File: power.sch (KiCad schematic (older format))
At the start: 5 parts

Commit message: added voltage regulators and FT231XS to drone library
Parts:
- removed J?: MOTOR_DRIVER, symbol Connector:Conn_01x02_Male
- removed U?: D36V50F5, Drone:D36V50F5, symbol Drone:D36V50F5
- added J?: XT60PW-M, Drone:XT60PW-M, symbol Drone:XT60PW-M
- added U?: D36V28F3, symbol Drone:D36V28F3
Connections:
- net labels added: 3V3, 5V
- wire segments 9 -> 35
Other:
- note added: "1. PG low battery indicator? (open drain and external pull up resistor is required)\n2. Enabled by default so EN shouldnt be wired?\n3. any capacitors missing?"
- note added: "Motor_Driver_Connector"
- moved on the sheet: SSR?, U?
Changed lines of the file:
@@
 $Descr A4 11693 8268
 encoding utf-8
-Sheet 4 6
+Sheet 4 5
 Title ""
 Date ""
@@
 L Drone:CMX60D20 SSR?
 U 1 1 5E3F8AD0
-P 4650 1150
+P 5900 1500
 AR Path="/5E3F8AD0" Ref="SSR?"  Part="1"
 AR Path="/5E3E92F4/5E3F8AD0" Ref="U?"  Part="1"
-F 0 "U?" H 4450 1300 50  0000 C CNN
-F 1 "CMX60D20" H 4600 1200 50  0000 C CNN
-F 2 "Drone:CMX60D20" H 4550 1150 50  0001 L BNN
-F 3 "https://www.tme.com/Document/b27c1a9b330ca081d5500ebe72e3b05d/c_m_x.pdf" H 4650 1150 50  0001 C CNN
-	1    4650 1150
+F 0 "U?" H 5700 1650 50  0000 C CNN
+F 1 "CMX60D20" H 5850 1550 50  0000 C CNN
+F 2 "Drone:CMX60D20" H 5800 1500 50  0001 L BNN
+F 3 "https://www.tme.com/Document/b27c1a9b330ca081d5500ebe72e3b05d/c_m_x.pdf" H 5900 1500 50  0001 C CNN
+	1    5900 1500
 	1    0    0    -1
 $EndComp
-Text Label 3700 1300 0    50   ~ 0
+Text Label 4950 1650 0    50   ~ 0
 GND
 Wire Wire Line
-	3700 1300 4200 1300
-Text Label 3700 1200 0    50   ~ 0
+	4950 1650 5450 1650
+Text Label 4950 1550 0    50   ~ 0
 GPIO_3V3
-Text Label 3700 850  0    50   ~ 0
+Text Label 4950 1200 0    50   ~ 0
 11V1
-$Comp
-L Connector:Conn_01x02_Male J?
-U 1 1 5E3F8ADC
-P 5450 1400
-F 0 "J?" V 5512 1444 50  0000 L CNN
-F 1 "MOTOR_DRIVER" V 5603 1444 50  0000 L CNN
-F 2 "" H 5450 1400 50  0001 C CNN
-F 3 "~" H 5450 1400 50  0001 C CNN
-	1    5450 1400
-	-1   0    0    1
-$EndComp
-Text Label 5100 1950 1    50   ~ 0
+Text Label 6500 1150 3    50   ~ 0
 GND
 $Comp
 L Drone:XT60PW-M J?
 U 1 1 5E3FF515
-P 1150 1100
+P 1600 4000
 AR Path="/5E3FF515" Ref="J?"  Part="1"
 AR Path="/5E3E92F4/5E3FF515" Ref="J?"  Part="1"
-F 0 "J?" H 1043 733 50  0000 C CNN
-F 1 "XT60PW-M" H 1043 824 50  0000 C CNN
-F 2 "Drone:XT60PW-M" H 1100 1400 50  0001 L BNN
-F 3 "https://www.snapeda.com/parts/XT60PW-M%20/AMASS/datasheet/" H 1100 1200 50  0001 L BNN
-	1    1150 1100
+F 0 "J?" H 1493 3633 50  0000 C CNN
+F 1 "XT60PW-M" H 1493 3724 50  0000 C CNN
+F 2 "Drone:XT60PW-M" H 1550 4300 50  0001 L BNN
+F 3 "https://www.snapeda.com/parts/XT60PW-M%20/AMASS/datasheet/" H 1550 4100 50  0001 L BNN
+	1    1600 4000
 	-1   0    0    1
 $EndComp
-Text Label 1850 1000 2    50   ~ 0
+Text Label 2300 3900 2    50   ~ 0
 11V1
 Wire Wire Line
-	1850 1200 1550 1200
-Text Label 1850 1200 2    50   ~ 0
+	2300 4100 2000 4100
+Text Label 2300 4100 2    50   ~ 0
 GND
 Wire Wire Line
-	1850 1000 1550 1000
+	2300 3900 2000 3900
 Wire Wire Line
-	4200 1200 3700 1200
+	5450 1550 4950 1550
 Wire Wire Line
-	5100 850  5100 1200
+	6350 1200 6350 1550
 Wire Wire Line
-	3700 850  5100 850
+	4950 1200 6350 1200
 Wire Wire Line
-	5100 1300 5250 1300
-Wire Wire Line
-	5250 1400 5100 1400
-Wire Wire Line
-	5100 1400 5100 1950
+	6350 1650 6500 1650
 $Comp
 L Drone:D36V50F5 U?
 U 1 1 5E3ABE9B
-P 2650 3000
-AR Path="/5E3ABE9B" Ref="U?"  Part="1"
-AR Path="/5E3E92F4/5E3ABE9B" Ref="U?"  Part="1"
-F 0 "U?" H 2650 2577 50  0000 C CNN
-F 1 "D36V50F5" H 2650 2486 50  0000 C CNN
-F 2 "Drone:D36V50F5" H 2600 2950 50  0001 C CNN
-F 3 "https://www.pololu.com/product/4091" H 2600 2950 50  0001 C CNN
-	1    2650 3000
+P 5150 3700
+F 0 "U?" H 5150 3650 50  0000 C CNN
+F 1 "D36V50F5" H 5150 3750 50  0000 C CNN
+F 2 "Drone:D36V50F5" H 5100 3650 50  0001 C CNN
+F 3 "https://www.pololu.com/product/4091" H 5100 3650 50  0001 C CNN
+	1    5150 3700
 	1    0    0    -1
 $EndComp
+Text Label 4300 3600 0    50   ~ 0
+11V1
+Text Label 6650 3550 0    50   ~ 0
+11V1
+Wire Wire Line
+	6650 3550 7050 3550
+Text Label 6800 4000 1    50   ~ 0
+GND
+Wire Wire Line
+	6800 3750 7050 3750
+Wire Wire Line
+	6800 3750 6800 4000
+Text Label 6000 3600 2    50   ~ 0
+5V
+Wire Wire Line
+	5700 3600 5750 3600
+Text Label 5100 4800 1    50   ~ 0
+GND
+Wire Wire Line
+	5400 4150 5400 4300
+Wire Wire Line
+	5400 4300 5250 4300
+Wire Wire Line
+	5100 4300 5100 4400
+Wire Wire Line
+	5100 4150 5100 4300
+Connection ~ 5100 4300
+Wire Wire Line
+	5250 4150 5250 4300
+Connection ~ 5250 4300
+Wire Wire Line
+	5250 4300 5100 4300
+Wire Wire Line
+	4950 4150 4950 4400
+Wire Wire Line
+	4950 4400 5100 4400
+Connection ~ 5100 4400
+Wire Wire Line
+	5100 4400 5100 4800
+Wire Wire Line
+	4300 3600 4550 3600
+Wire Wire Line
+	4550 3600 4550 3800
+Wire Wire Line
+	4550 3800 4600 3800
+Connection ~ 4550 3600
+Wire Wire Line
+	4550 3600 4600 3600
+Wire Wire Line
+	5700 3800 5750 3800
+Wire Wire Line
+	5750 3800 5750 3600
+Connection ~ 5750 3600
+Wire Wire Line
+	5750 3600 6000 3600
+Text Notes 4750 5200 0    50   ~ 0
+1. PG low battery indicator? (open drain and external pull up resistor is required)\n2. Enabled by default so EN shouldnt be wired?\n3. any capacitors missing?
+Wire Wire Line
+	8150 3550 8400 3550
+Text Label 8400 3550 2    50   ~ 0
+3V3
 $Comp
-L Drone:D36V50F5 U?
-U 1 1 5E3AC357
-P 4950 3000
-AR Path="/5E3AC357" Ref="U?"  Part="1"
-AR Path="/5E3E92F4/5E3AC357" Ref="U?"  Part="1"
-F 0 "U?" H 4950 2577 50  0000 C CNN
-F 1 "D36V50F5" H 4950 2486 50  0000 C CNN
-F 2 "Drone:D36V50F5" H 4900 2950 50  0001 C CNN
-F 3 "https://www.pololu.com/product/4091" H 4900 2950 50  0001 C CNN
-	1    4950 3000
+L Drone:D36V28F3 U?
+U 1 1 5E3B18FA
+P 7600 3650
+F 0 "U?" H 7600 3750 50  0000 C CNN
+F 1 "D36V28F3" H 7600 3600 50  0000 C CNN
+F 2 "" H 7550 3600 50  0001 C CNN
+F 3 "https://www.pololu.com/product/3781" H 7550 3600 50  0001 C CNN
+	1    7600 3650
 	1    0    0    -1
 $EndComp
+Wire Wire Line
+	8150 3750 8150 4100
+Wire Wire Line
+	8150 4100 7050 4100
+Wire Wire Line
+	7050 4100 7050 3750
+Connection ~ 7050 3750
+Text HLabel 10900 6000 2    50   Output ~ 0
+5V
+Text HLabel 10900 6100 2    50   Output ~ 0
+3V3
+Text HLabel 10900 6200 2    50   Output ~ 0
+GND
+Wire Wire Line
+	10900 6000 10650 6000
+Wire Wire Line
+	10900 6100 10650 6100
+Wire Wire Line
+	10900 6200 10650 6200
+Text Label 10650 6200 0    50   ~ 0
+GND
+Text Label 10650 6100 0    50   ~ 0
+3V3
+Text Label 10650 6000 0    50   ~ 0
+5V
+$Comp
+L Drone:XT60PW-M J?
+U 1 1 5E4231A4
+P 6900 1550
+AR Path="/5E4231A4" Ref="J?"  Part="1"
+AR Path="/5E3E92F4/5E4231A4" Ref="J?"  Part="1"
+F 0 "J?" H 6793 1183 50  0000 C CNN
+F 1 "XT60PW-M" H 6793 1274 50  0000 C CNN
+F 2 "Drone:XT60PW-M" H 6850 1850 50  0001 L BNN
+F 3 "https://www.snapeda.com/parts/XT60PW-M%20/AMASS/datasheet/" H 6850 1650 50  0001 L BNN
+	1    6900 1550
+	1    0    0    -1
+$EndComp
+Wire Wire Line
+	6500 1150 6500 1450
+Text Notes 6650 1300 0    50   ~ 0
+Motor_Driver_Connector
 $EndSCHEMATC

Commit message: added connectors symbols and footprints
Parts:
- removed J? (x2): XT60PW-M, Drone:XT60PW-M, symbol Drone:XT60PW-M
- added J?: XT90PW-M, Drone:XT90PW-M, symbol Drone:XT90PW-M
- added J?: XT60PW-F_Vertical, Drone:AMASS_XT60-F_1x02_P7.20mm_Vertical, symbol Drone:XT60PW-F_Vertical
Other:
- note added: "TODO: \n2. check what top level components are necessary (voltage regulators & stepdown?)\n4. Replace motor driver 2 pin male connector with a proper connector\n5. Check connectors orientation\n"
- note removed: "TODO: \n1. batt connector to switch (maybe not)\n2. check what top level components are necessary (voltage regulators & stepdown?)\n3. CMX60D20 connection to motor board (double check symbol)\n4. Replace motor driver 2 pin male connector with a proper connector\n5. check XT60PW and CMX60D20 connections (connect to proper GPIO)"
- moved on the sheet: SSR?
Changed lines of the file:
@@
 $Descr A4 11693 8268
 encoding utf-8
-Sheet 2 6
+Sheet 6 6
 Title ""
 Date ""
@@
 Comment4 ""
 $EndDescr
-Text Notes 7750 1200 0    50   ~ 0
-TODO: \n1. batt connector to switch (maybe not)\n2. check what top level components are necessary (voltage regulators & stepdown?)\n3.  CMX60D20 connection to motor board (double check symbol)\n4. Replace motor driver 2 pin male connector with a proper connector\n5. check XT60PW and CMX60D20 connections (connect to proper GPIO)
+Text Notes 5950 1700 0    50   ~ 0
+TODO: \n2. check what top level components are necessary (voltage regulators & stepdown?)\n4. Replace motor driver 2 pin male connector with a proper connector\n5. Check connectors orientation\n
 $Comp
 L Drone:CMX60D20 SSR?
 U 1 1 5E3F8AD0
-P 5900 1500
+P 3300 1350
 AR Path="/5E3F8AD0" Ref="SSR?"  Part="1"
 AR Path="/5E3E92F4/5E3F8AD0" Ref="U?"  Part="1"
-F 0 "U?" H 5700 1650 50  0000 C CNN
-F 1 "CMX60D20" H 5850 1550 50  0000 C CNN
-F 2 "Drone:CMX60D20" H 5800 1500 50  0001 L BNN
-F 3 "https://www.tme.com/Document/b27c1a9b330ca081d5500ebe72e3b05d/c_m_x.pdf" H 5900 1500 50  0001 C CNN
-	1    5900 1500
+F 0 "U?" H 3100 1500 50  0000 C CNN
+F 1 "CMX60D20" H 3250 1400 50  0000 C CNN
+F 2 "Drone:CMX60D20" H 3200 1350 50  0001 L BNN
+F 3 "https://www.tme.com/Document/b27c1a9b330ca081d5500ebe72e3b05d/c_m_x.pdf" H 3300 1350 50  0001 C CNN
+	1    3300 1350
 	1    0    0    -1
 $EndComp
-Text Label 4950 1650 0    50   ~ 0
+Text Label 2350 1500 0    50   ~ 0
 GND
 Wire Wire Line
-	4950 1650 5450 1650
-Text Label 4950 1550 0    50   ~ 0
+	2350 1500 2850 1500
+Text Label 2350 1400 0    50   ~ 0
 GPIO_3V3
-Text Label 4950 1200 0    50   ~ 0
+Text Label 2350 1050 0    50   ~ 0
 11V1
-Text Label 6500 1150 3    50   ~ 0
+Text Label 3900 1000 3    50   ~ 0
 GND
-$Comp
-L Drone:XT60PW-M J?
-U 1 1 5E3FF515
-P 1600 4000
-AR Path="/5E3FF515" Ref="J?"  Part="1"
-AR Path="/5E3E92F4/5E3FF515" Ref="J?"  Part="1"
-F 0 "J?" H 1493 3633 50  0000 C CNN
-F 1 "XT60PW-M" H 1493 3724 50  0000 C CNN
-F 2 "Drone:XT60PW-M" H 1550 4300 50  0001 L BNN
-F 3 "https://www.snapeda.com/parts/XT60PW-M%20/AMASS/datasheet/" H 1550 4100 50  0001 L BNN
-	1    1600 4000
-	-1   0    0    1
-$EndComp
-Text Label 2300 3900 2    50   ~ 0
+Text Label 1900 1300 2    50   ~ 0
 11V1
 Wire Wire Line
-	2300 4100 2000 4100
-Text Label 2300 4100 2    50   ~ 0
+	1900 1500 1600 1500
+Text Label 1900 1500 2    50   ~ 0
 GND
 Wire Wire Line
-	2300 3900 2000 3900
+	1900 1300 1600 1300
 Wire Wire Line
-	5450 1550 4950 1550
+	2850 1400 2350 1400
 Wire Wire Line
-	6350 1200 6350 1550
+	3750 1050 3750 1400
 Wire Wire Line
-	4950 1200 6350 1200
+	2350 1050 3750 1050
 Wire Wire Line
-	6350 1650 6500 1650
+	3750 1500 3900 1500
 $Comp
 L Drone:D36V50F5 U?
@@
 Text Label 10650 6000 0    50   ~ 0
 5V
+Wire Wire Line
+	3900 1000 3900 1300
+Text Notes 3950 1150 0    50   ~ 0
+Motor_Driver_Connector
 $Comp
-L Drone:XT60PW-M J?
-U 1 1 5E4231A4
-P 6900 1550
-AR Path="/5E4231A4" Ref="J?"  Part="1"
-AR Path="/5E3E92F4/5E4231A4" Ref="J?"  Part="1"
-F 0 "J?" H 6793 1183 50  0000 C CNN
-F 1 "XT60PW-M" H 6793 1274 50  0000 C CNN
-F 2 "Drone:XT60PW-M" H 6850 1850 50  0001 L BNN
-F 3 "https://www.snapeda.com/parts/XT60PW-M%20/AMASS/datasheet/" H 6850 1650 50  0001 L BNN
-	1    6900 1550
+L Drone:XT90PW-M J?
+U 1 1 5E3D24EA
+P 1200 1400
+F 0 "J?" H 1093 1033 50  0000 C CNN
+F 1 "XT90PW-M" H 1093 1124 50  0000 C CNN
+F 2 "Drone:XT90PW-M" H 1100 1650 50  0001 L BNN
+F 3 "" H 1150 1500 50  0001 L BNN
+	1    1200 1400
+	-1   0    0    1
+$EndComp
+$Comp
+L Drone:XT60PW-F_Vertical J?
+U 1 1 5E3DE251
+P 4300 1400
+F 0 "J?" H 4530 1446 50  0000 L CNN
+F 1 "XT60PW-F_Vertical" H 4530 1355 50  0000 L CNN
+F 2 "Drone:AMASS_XT60-F_1x02_P7.20mm_Vertical" H 4200 1650 50  0001 L BNN
+F 3 "" H 4250 1500 50  0001 L BNN
+	1    4300 1400
 	1    0    0    -1
 $EndComp
-Wire Wire Line
-	6500 1150 6500 1450
-Text Notes 6650 1300 0    50   ~ 0
-Motor_Driver_Connector
 $EndSCHEMATC

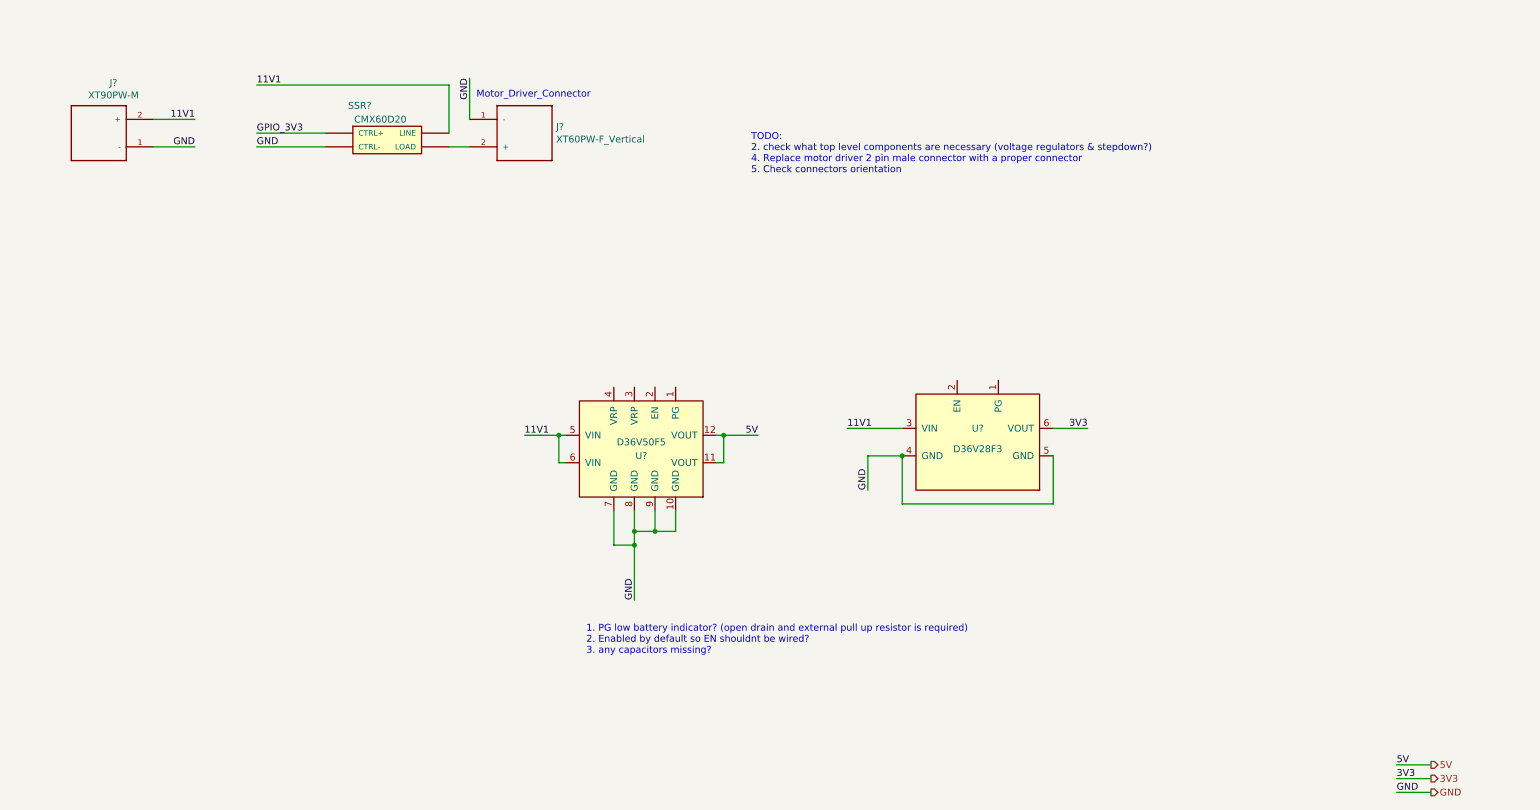
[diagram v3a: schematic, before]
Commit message: added 1.8V and 2.8V LDOs
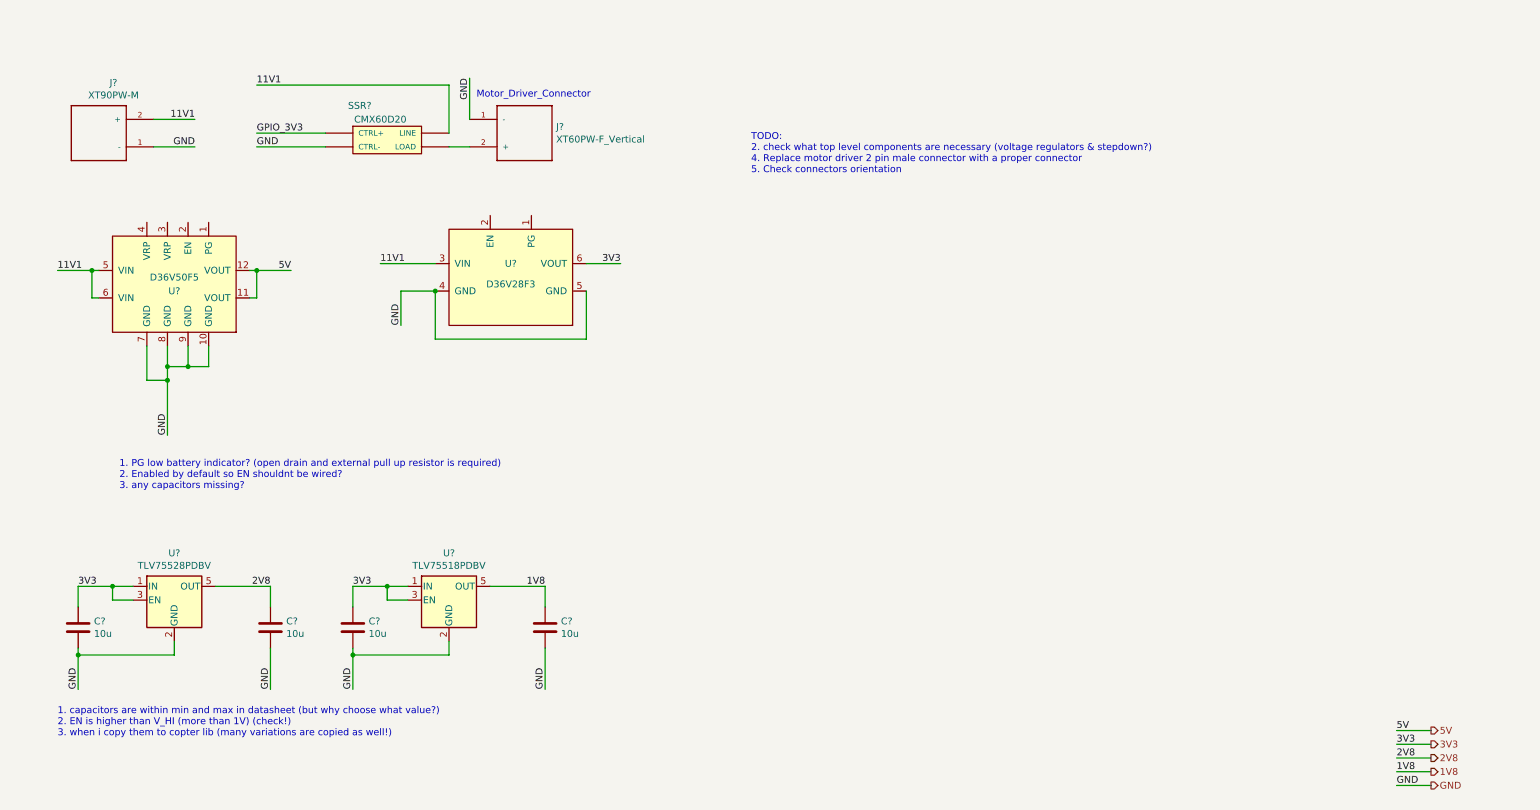
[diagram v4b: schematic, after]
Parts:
- added C? (x4): 10u, symbol Device:C
- added U?: TLV75528PDBV, Package_TO_SOT_SMD:SOT-23-5, symbol Regulator_Linear:TLV75528PDBV
- added U?: TLV75518PDBV, Package_TO_SOT_SMD:SOT-23-5, symbol Regulator_Linear:TLV75518PDBV
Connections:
- net 3V3: now also C?.1, C?.1, U?.1 (IN), U?.1 (IN), U?.3 (EN), U?.3 (EN)
- net GND: now also C?.2, C?.2, C?.2, C?.2, U?.2 (GND), U?.2 (GND)
- new net 1V8: C?.1, U?.5 (OUT)
- new net 2V8: C?.1, U?.5 (OUT)
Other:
- note added: "1. capacitors are within min and max in datasheet (but why choose what value?)\n2. EN is higher than V_HI (more than 1V) (check!)\n3. when i copy them to copter lib (many variations are copied as well!)"
- moved on the sheet: U?

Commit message: added missing 3d models and other minor changes
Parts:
- J?: footprint Drone:AMASS_XT60-F_1x02_P7.20mm_Vertical -> Drone:XT60-F_1x02_P7.20mm_Vertical
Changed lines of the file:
@@
 F 0 "J?" H 4530 1446 50  0000 L CNN
 F 1 "XT60PW-F_Vertical" H 4530 1355 50  0000 L CNN
-F 2 "Drone:AMASS_XT60-F_1x02_P7.20mm_Vertical" H 4200 1650 50  0001 L BNN
+F 2 "Drone:XT60-F_1x02_P7.20mm_Vertical" H 4200 1650 50  0001 L BNN
 F 3 "" H 4250 1500 50  0001 L BNN
 	1    4300 1400

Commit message: Use 0805 for all capacitors and resistors.
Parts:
- C? (x4): footprint (none) -> Capacitor_SMD:C_0805_2012Metric_Pad1.15x1.40mm_HandSolder; symbol Device:C -> Drone:CAP
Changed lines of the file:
@@
 	2050 4700 2450 4700
 $Comp
-L Device:C C?
+L Drone:CAP C?
 U 1 1 5E40BD7D
 P 1050 5000
@@
 F 0 "C?" H 1165 5046 50  0000 L CNN
 F 1 "10u" H 1165 4955 50  0000 L CNN
-F 2 "" H 1088 4850 50  0001 C CNN
+F 2 "Capacitor_SMD:C_0805_2012Metric_Pad1.15x1.40mm_HandSolder" H 1088 4850 50  0001 C CNN
 F 3 "~" H 1050 5000 50  0001 C CNN
 	1    1050 5000
@@
 	1050 4700 1050 4850
 $Comp
-L Device:C C?
+L Drone:CAP C?
 U 1 1 5E41DB5A
 P 2450 5000
@@
 F 0 "C?" H 2565 5046 50  0000 L CNN
 F 1 "10u" H 2565 4955 50  0000 L CNN
-F 2 "" H 2488 4850 50  0001 C CNN
+F 2 "Capacitor_SMD:C_0805_2012Metric_Pad1.15x1.40mm_HandSolder" H 2488 4850 50  0001 C CNN
 F 3 "~" H 2450 5000 50  0001 C CNN
 	1    2450 5000
@@
 	4050 4700 4450 4700
 $Comp
-L Device:C C?
+L Drone:CAP C?
 U 1 1 5E4477D8
 P 3050 5000
@@
 F 0 "C?" H 3165 5046 50  0000 L CNN
 F 1 "10u" H 3165 4955 50  0000 L CNN
-F 2 "" H 3088 4850 50  0001 C CNN
+F 2 "Capacitor_SMD:C_0805_2012Metric_Pad1.15x1.40mm_HandSolder" H 3088 4850 50  0001 C CNN
 F 3 "~" H 3050 5000 50  0001 C CNN
 	1    3050 5000
@@
 	3050 4700 3050 4850
 $Comp
-L Device:C C?
+L Drone:CAP C?
 U 1 1 5E4477E2
 P 4450 5000
@@
 F 0 "C?" H 4565 5046 50  0000 L CNN
 F 1 "10u" H 4565 4955 50  0000 L CNN
-F 2 "" H 4488 4850 50  0001 C CNN
+F 2 "Capacitor_SMD:C_0805_2012Metric_Pad1.15x1.40mm_HandSolder" H 4488 4850 50  0001 C CNN
 F 3 "~" H 4450 5000 50  0001 C CNN
 	1    4450 5000
